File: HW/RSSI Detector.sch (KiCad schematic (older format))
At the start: 13 parts

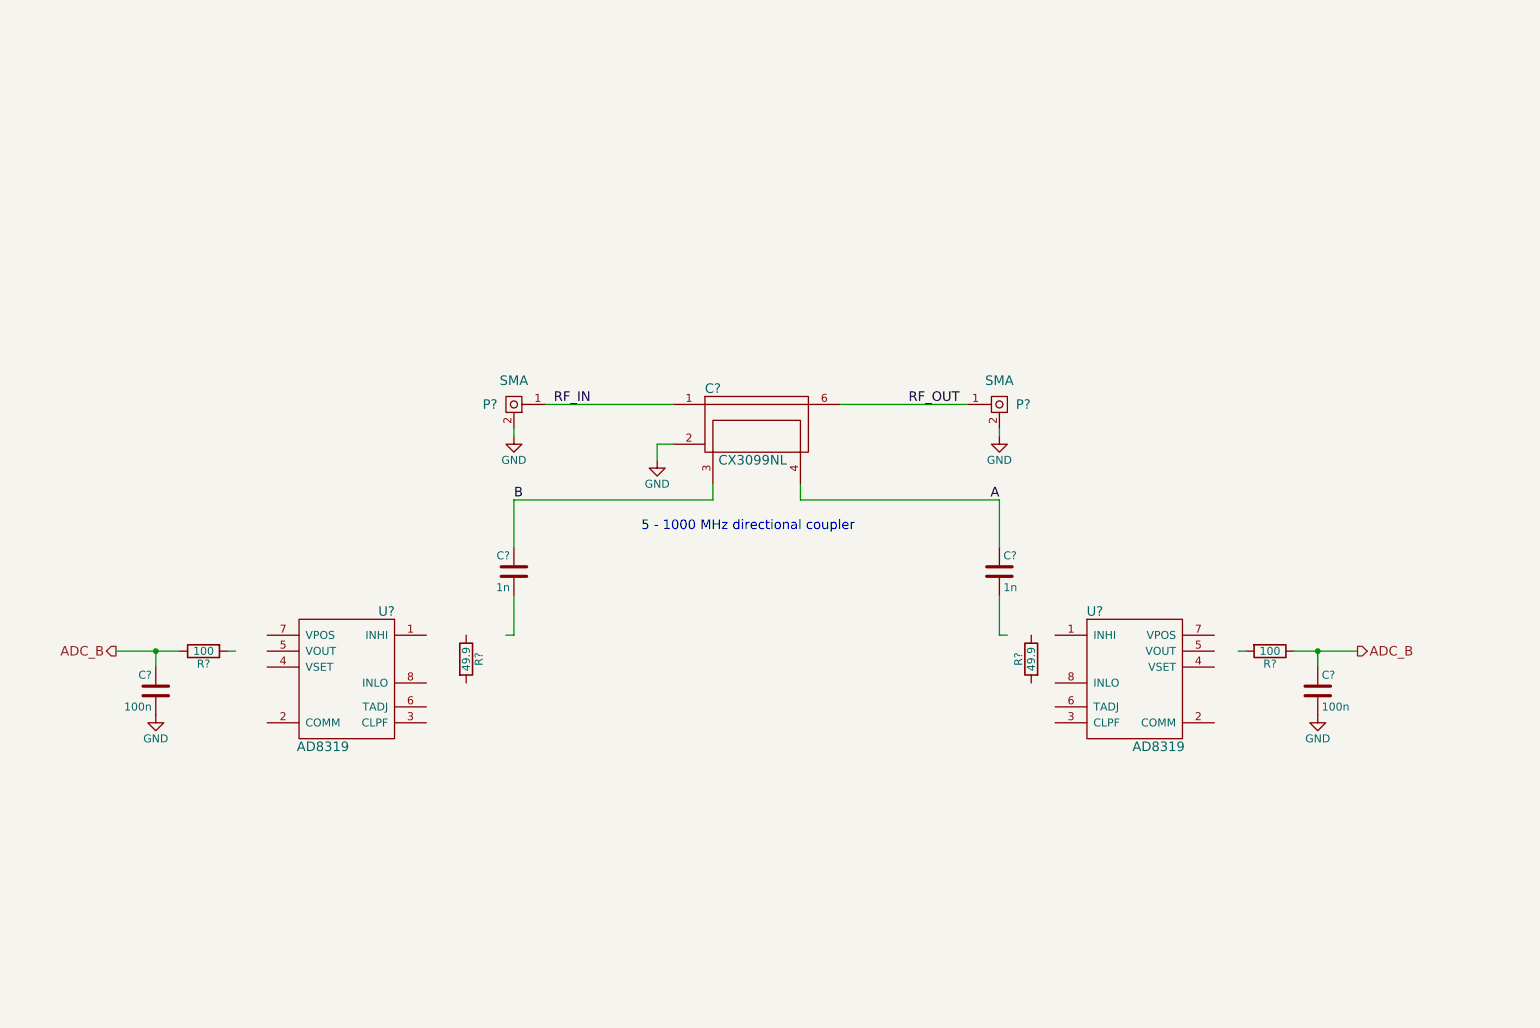
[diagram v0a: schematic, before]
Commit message: finished sch, footprints done
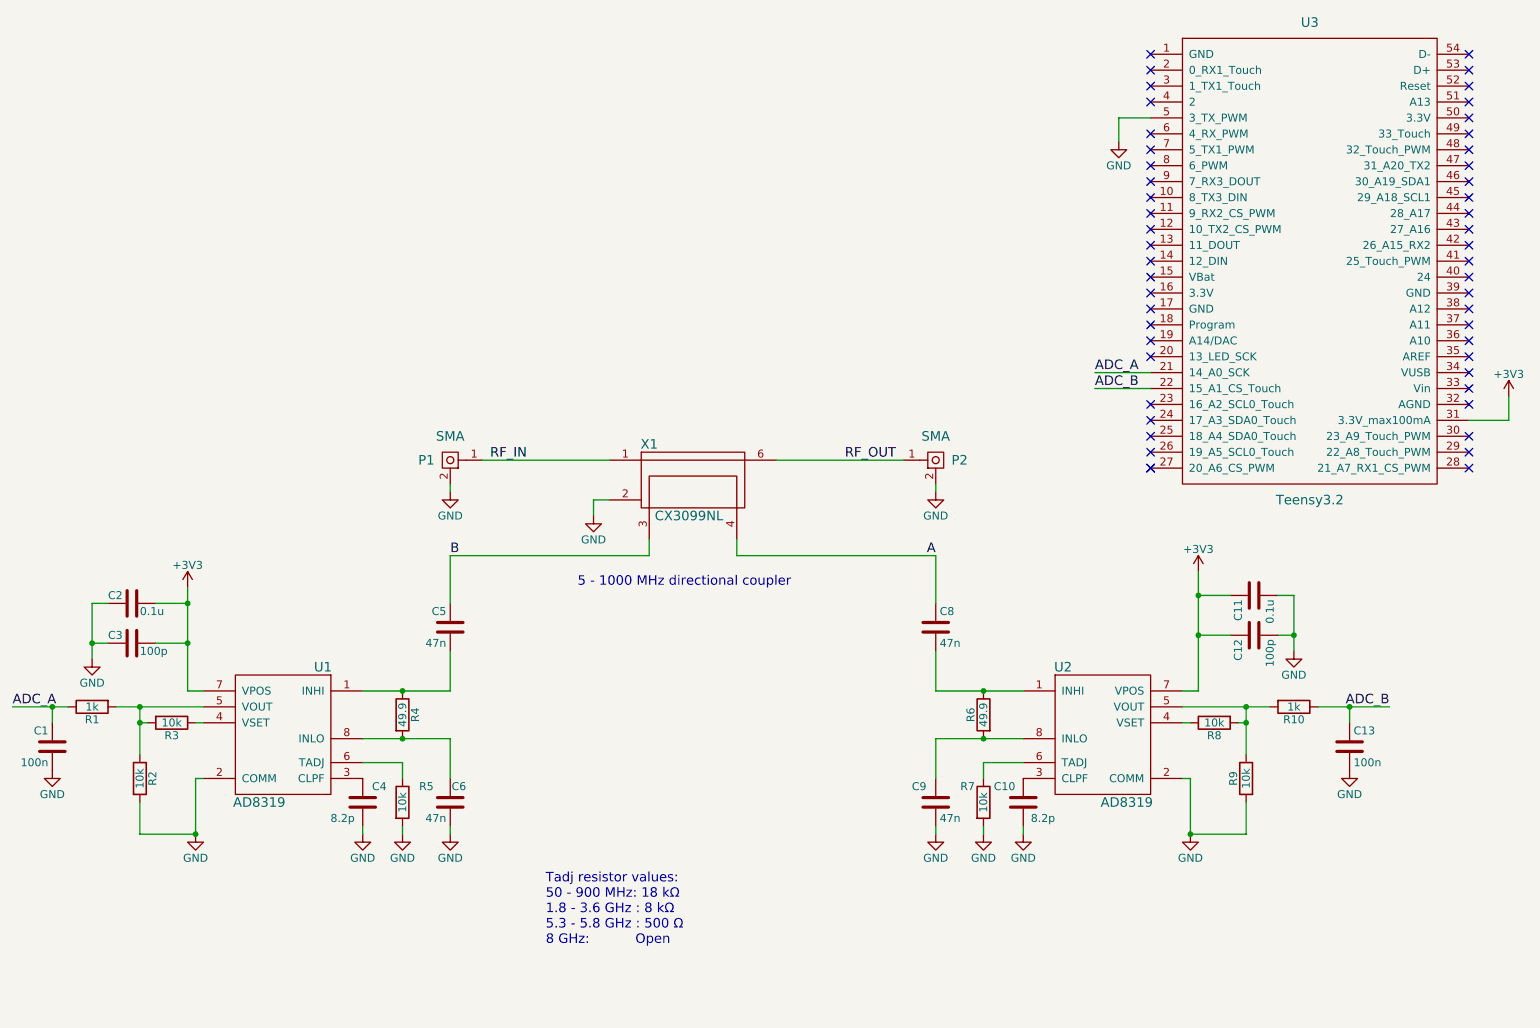
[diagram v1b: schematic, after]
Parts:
- added C10, C4: 8.2p, vna:C_0402b, symbol C
- added C11, C2: 0.1u, vna:C_0603b, symbol C
- added C12, C3: 100p, vna:C_0402b, symbol C
- added C6, C9: 47n, VNA:C_0402b, symbol C
- added R2, R3, R5, R7, R8, R9: 10k, vna:R_0603b, symbol R
- added U3: Teensy3.2, vna:Teensy30_31_32_LC_modified, symbol Teensy3.2
- C1, C13: renamed from C?; footprint VNA:C_0402b -> vna:C_0603b
- C5, C8: renamed from C?; value 1n -> 47n
- P1, P2: renamed from P?; footprint (none) -> vna:CONSMA003.062
- R1, R10: renamed from R?; value 100 -> 1k
- R4, R6: renamed from R?; footprint Resistors_SMD:R_0603 -> vna:R_0402b
- U1, U2: renamed from U?; footprint (none) -> vna:8-LFCSP_VD
- X1: renamed from C?; footprint (none) -> vna:CX3099NL
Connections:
- net labels added: +3V3, ADC_A
- wire segments 22 -> 70
- no-connect marks 0 -> 51
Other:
- note added: "Tadj resistor values:\n50 - 900 MHz: 18 kΩ\n1.8 - 3.6 GHz : 8 kΩ\n5.3 - 5.8 GHz : 500 Ω\n8 GHz: Open"
- moved on the sheet: C1, C13, C5, C8, P1, P2, R1, R10, R4, R6, U1, U2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

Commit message: prelim placement
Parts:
- C10, C12, C3, C4: footprint vna:C_0402b -> vna:C_0603b
- C5, C6, C8, C9: footprint VNA:C_0402b -> vna:C_0402b
- R1, R10: footprint VNA:R_0402b -> Resistors_SMD:R_0603
- R2, R3, R5, R7, R8, R9: footprint vna:R_0603b -> Resistors_SMD:R_0603
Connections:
- net A: now also C8.2, R6.1; no longer C8.1
- net B: now also R4.1
- net GND: now also C6.1, R4.2, R6.2; no longer C6.2
- net at C5.2, U1.1 (INHI): no longer R4.1
- net at C9.1, U2.8 (INLO): no longer R6.2
- new net: C8.1, U2.1 (INHI)
- new net: C6.2, U1.8 (INLO)
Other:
- moved on the sheet: C5, C6, C8, C9, R4, R6
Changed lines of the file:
@@
 L R R4
 U 1 1 59C23EFC
-P 3900 5050
-F 0 "R4" V 3980 5050 50  0000 C CNN
-F 1 "49.9" V 3900 5050 50  0000 C CNN
-F 2 "vna:R_0402b" V 3830 5050 30  0001 C CNN
-F 3 "" H 3900 5050 30  0000 C CNN
-	1    3900 5050
+P 4200 5050
+F 0 "R4" V 4280 5050 50  0000 C CNN
+F 1 "49.9" V 4200 5050 50  0000 C CNN
+F 2 "vna:R_0402b" V 4130 5050 30  0001 C CNN
+F 3 "" H 4200 5050 30  0000 C CNN
+	1    4200 5050
 	1    0    0    -1
 $EndComp
@@
 A
 $Comp
-L C C8
-U 1 1 59C23F21
-P 7250 4500
-F 0 "C8" H 7275 4600 50  0000 L CNN
-F 1 "47n" H 7275 4400 50  0000 L CNN
-F 2 "VNA:C_0402b" H 7288 4350 30  0001 C CNN
-F 3 "" H 7250 4500 60  0000 C CNN
-	1    7250 4500
-	1    0    0    -1
-$EndComp
-$Comp
-L C C5
-U 1 1 59C23F6A
-P 4200 4500
-F 0 "C5" H 4225 4600 50  0000 L CNN
-F 1 "47n" H 4225 4400 50  0000 L CNN
-F 2 "VNA:C_0402b" H 4238 4350 30  0001 C CNN
-F 3 "" H 4200 4500 60  0000 C CNN
-	1    4200 4500
-	-1   0    0    -1
-$EndComp
-$Comp
 L R R1
 U 1 1 59C23F92
@@
 F 0 "R1" V 2030 5000 50  0000 C CNN
 F 1 "1k" V 1950 5000 50  0000 C CNN
-F 2 "VNA:R_0402b" V 1880 5000 30  0001 C CNN
+F 2 "Resistors_SMD:R_0603" V 1880 5000 30  0001 C CNN
 F 3 "" H 1950 5000 30  0000 C CNN
 	1    1950 5000
@@
 L R R6
 U 1 1 59C2507D
-P 7550 5050
-F 0 "R6" V 7630 5050 50  0000 C CNN
-F 1 "49.9" V 7550 5050 50  0000 C CNN
-F 2 "vna:R_0402b" V 7480 5050 30  0001 C CNN
-F 3 "" H 7550 5050 30  0000 C CNN
-	1    7550 5050
+P 7250 5050
+F 0 "R6" V 7330 5050 50  0000 C CNN
+F 1 "49.9" V 7250 5050 50  0000 C CNN
+F 2 "vna:R_0402b" V 7180 5050 30  0001 C CNN
+F 3 "" H 7250 5050 30  0000 C CNN
+	1    7250 5050
 	-1   0    0    -1
 $EndComp
@@
 F 0 "R10" V 9580 5000 50  0000 C CNN
 F 1 "1k" V 9500 5000 50  0000 C CNN
-F 2 "VNA:R_0402b" V 9430 5000 30  0001 C CNN
+F 2 "Resistors_SMD:R_0603" V 9430 5000 30  0001 C CNN
 F 3 "" H 9500 5000 30  0000 C CNN
 	1    9500 5000
@@
 F 0 "C3" V 2150 4450 50  0000 L CNN
 F 1 "100p" V 2250 4650 50  0000 L CNN
-F 2 "vna:C_0402b" H 2238 4450 50  0001 C CNN
+F 2 "vna:C_0603b" H 2238 4450 50  0001 C CNN
 F 3 "" H 2200 4600 50  0001 C CNN
 	1    2200 4600
@@
 	6000 3950 6000 4050
 Wire Wire Line
-	7250 4650 7250 4900
-Wire Wire Line
-	7250 4900 7800 4900
+	7250 4050 7250 4900
 Wire Wire Line
 	6000 4050 7250 4050
 Wire Wire Line
-	7250 4050 7250 4350
-Wire Wire Line
-	4200 4900 4200 4650
-Wire Wire Line
-	3650 4900 4200 4900
+	4200 4050 4200 4900
 Wire Wire Line
 	2100 5000 2650 5000
@@
 Wire Wire Line
 	5450 4050 4200 4050
-Wire Wire Line
-	4200 4050 4200 4350
 Wire Wire Line
 	1700 5000 1700 5100
@@
 Wire Wire Line
 	4200 3600 4200 3650
-Connection ~ 3900 4900
-Wire Wire Line
-	3650 5200 4200 5200
-Connection ~ 7550 4900
-Wire Wire Line
-	7250 5200 7800 5200
+Connection ~ 4200 4900
+Connection ~ 7250 4900
+Wire Wire Line
+	7250 5200 7400 5200
 Wire Wire Line
 	2650 5100 2600 5100
@@
 F 0 "C12" H 9275 4650 50  0000 L CNN
 F 1 "100p" H 9275 4450 50  0000 L CNN
-F 2 "vna:C_0402b" H 9288 4400 50  0001 C CNN
+F 2 "vna:C_0603b" H 9288 4400 50  0001 C CNN
 F 3 "" H 9250 4550 50  0001 C CNN
 	1    9250 4550
@@
 L C C6
 U 1 1 59C28F3F
-P 4200 5600
-F 0 "C6" H 4100 5700 50  0000 L CNN
-F 1 "47n" H 4225 5500 50  0000 L CNN
-F 2 "VNA:C_0402b" H 4238 5450 30  0001 C CNN
-F 3 "" H 4200 5600 60  0000 C CNN
-	1    4200 5600
-	-1   0    0    -1
-$EndComp
-Wire Wire Line
-	4200 5200 4200 5450
-Connection ~ 3900 5200
+P 3850 5200
+F 0 "C6" H 3750 5300 50  0000 L CNN
+F 1 "47n" H 3875 5100 50  0000 L CNN
+F 2 "vna:C_0402b" H 3888 5050 30  0001 C CNN
+F 3 "" H 3850 5200 60  0000 C CNN
+	1    3850 5200
+	0    1    -1   0
+$EndComp
+Wire Wire Line
+	4200 5200 4200 5800
+Connection ~ 4200 5200
 $Comp
 L C C9
 U 1 1 59C29280
-P 7250 5600
-F 0 "C9" H 7100 5700 50  0000 L CNN
-F 1 "47n" H 7275 5500 50  0000 L CNN
-F 2 "VNA:C_0402b" H 7288 5450 30  0001 C CNN
-F 3 "" H 7250 5600 60  0000 C CNN
-	1    7250 5600
-	1    0    0    -1
-$EndComp
-Wire Wire Line
-	7250 5200 7250 5450
-Connection ~ 7550 5200
+P 7550 5200
+F 0 "C9" H 7400 5300 50  0000 L CNN
+F 1 "47n" H 7575 5100 50  0000 L CNN
+F 2 "vna:C_0402b" H 7588 5050 30  0001 C CNN
+F 3 "" H 7550 5200 60  0000 C CNN
+	1    7550 5200
+	0    1    1    0
+$EndComp
+Wire Wire Line
+	7250 5200 7250 5800
+Connection ~ 7250 5200
 $Comp
 L R R5
@@
 F 0 "R5" H 4050 5700 50  0000 C CNN
 F 1 "10k" V 3900 5600 50  0000 C CNN
-F 2 "vna:R_0603b" V 3830 5600 30  0001 C CNN
+F 2 "Resistors_SMD:R_0603" V 3830 5600 30  0001 C CNN
 F 3 "" H 3900 5600 30  0000 C CNN
 	1    3900 5600
@@
 F 0 "R7" H 7450 5700 50  0000 C CNN
 F 1 "10k" V 7550 5600 50  0000 C CNN
-F 2 "vna:R_0603b" V 7480 5600 30  0001 C CNN
+F 2 "Resistors_SMD:R_0603" V 7480 5600 30  0001 C CNN
 F 3 "" H 7550 5600 30  0000 C CNN
 	1    7550 5600
@@
 F 0 "R2" V 2330 5450 50  0000 C CNN
 F 1 "10k" V 2250 5450 50  0000 C CNN
-F 2 "vna:R_0603b" V 2180 5450 30  0001 C CNN
+F 2 "Resistors_SMD:R_0603" V 2180 5450 30  0001 C CNN
 F 3 "" H 2250 5450 30  0000 C CNN
 	1    2250 5450
@@
 F 0 "R3" V 2530 5100 50  0000 C CNN
 F 1 "10k" V 2450 5100 50  0000 C CNN
-F 2 "vna:R_0603b" V 2380 5100 30  0001 C CNN
+F 2 "Resistors_SMD:R_0603" V 2380 5100 30  0001 C CNN
 F 3 "" H 2450 5100 30  0000 C CNN
 	1    2450 5100
@@
 F 0 "R9" V 9280 5450 50  0000 C CNN
 F 1 "10k" V 9200 5450 50  0000 C CNN
-F 2 "vna:R_0603b" V 9130 5450 30  0001 C CNN
+F 2 "Resistors_SMD:R_0603" V 9130 5450 30  0001 C CNN
 F 3 "" H 9200 5450 30  0000 C CNN
 	1    9200 5450
@@
 F 0 "R8" V 9080 5100 50  0000 C CNN
 F 1 "10k" V 9000 5100 50  0000 C CNN
-F 2 "vna:R_0603b" V 8930 5100 30  0001 C CNN
+F 2 "Resistors_SMD:R_0603" V 8930 5100 30  0001 C CNN
 F 3 "" H 9000 5100 30  0000 C CNN
 	1    9000 5100
@@
 F 0 "C4" H 3500 5500 50  0000 L CNN
 F 1 "8.2p" H 3700 5700 50  0000 L CNN
-F 2 "vna:C_0402b" H 3688 5450 50  0001 C CNN
+F 2 "vna:C_0603b" H 3688 5450 50  0001 C CNN
 F 3 "" H 3650 5600 50  0001 C CNN
 	1    3650 5600
@@
 F 0 "C10" H 7850 5500 50  0000 L CNN
 F 1 "8.2p" H 7600 5700 50  0000 L CNN
-F 2 "vna:C_0402b" H 7838 5450 50  0001 C CNN
+F 2 "vna:C_0603b" H 7838 5450 50  0001 C CNN
 F 3 "" H 7800 5600 50  0001 C CNN
 	1    7800 5600
@@
 Wire Wire Line
 	3900 5750 3900 5800
-Wire Wire Line
-	4200 5750 4200 5800
 $Comp
 L GND #PWR014
@@
 Wire Wire Line
 	7550 5750 7550 5800
-Wire Wire Line
-	7250 5750 7250 5800
 Wire Wire Line
 	8800 5450 8850 5450
@@
 NoConn ~ 8600 3300
 NoConn ~ 8600 3400
+$Comp
+L C C5
+U 1 1 59C23F6A
+P 3850 4900
+F 0 "C5" H 3875 5000 50  0000 L CNN
+F 1 "47n" H 3875 4800 50  0000 L CNN
+F 2 "vna:C_0402b" H 3888 4750 30  0001 C CNN
+F 3 "" H 3850 4900 60  0000 C CNN
+	1    3850 4900
+	0    1    -1   0
+$EndComp
+Wire Wire Line
+	4200 4900 4000 4900
+Wire Wire Line
+	3700 4900 3650 4900
+Wire Wire Line
+	3650 5200 3700 5200
+Wire Wire Line
+	4000 5200 4200 5200
+$Comp
+L C C8
+U 1 1 59C23F21
+P 7550 4900
+F 0 "C8" H 7575 5000 50  0000 L CNN
+F 1 "47n" H 7575 4800 50  0000 L CNN
+F 2 "vna:C_0402b" H 7588 4750 30  0001 C CNN
+F 3 "" H 7550 4900 60  0000 C CNN
+	1    7550 4900
+	0    1    1    0
+$EndComp
+Wire Wire Line
+	7250 4900 7400 4900
+Wire Wire Line
+	7700 4900 7800 4900
+Wire Wire Line
+	7700 5200 7800 5200
 $EndSCHEMATC

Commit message: put Henrik's coupler
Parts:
- removed X1: CX3099NL, vna:CX3099NL, symbol CX3099NL
- added F?: COUPLER, symbol COUPLER
- added R? (x2): 49.9, vna:R_0402b, symbol R
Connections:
- net A: now also F?.6
- net B: now also F?.3
- net GND: now also F?.GND, R?.2, R?.2
- net RF_IN: now also F?.1
- net RF_OUT: now also F?.2
- new net: F?.4, R?.1
- new net: F?.5, R?.1
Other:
- note removed: "5 - 1000 MHz directional coupler"
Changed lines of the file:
@@
 $EndComp
-$Comp
-L CX3099NL X1
-U 1 1 59C262AE
-P 5750 3550
-F 0 "X1" H 5450 3750 60  0000 C CNN
-F 1 "CX3099NL" H 5700 3300 60  0000 C CNN
-F 2 "vna:CX3099NL" H 5750 3650 60  0001 C CNN
-F 3 "" H 5750 3650 60  0000 C CNN
-	1    5750 3550
-	1    0    0    -1
-$EndComp
-Text Notes 5000 4250 0    60   ~ 0
-5 - 1000 MHz directional coupler
 $Comp
 L SMA P1
@@
 Wire Wire Line
 	7700 5200 7800 5200
+$Comp
+L COUPLER F?
+U 1 1 59CC1068
+P 5750 3550
+F 0 "F?" H 6200 3400 60  0000 C CNN
+F 1 "COUPLER" H 5650 3800 60  0000 C CNN
+F 2 "" H 5750 3650 60  0000 C CNN
+F 3 "" H 5750 3650 60  0000 C CNN
+	1    5750 3550
+	1    0    0    -1
+$EndComp
+$Comp
+L R R?
+U 1 1 59CC14B8
+P 5650 4200
+F 0 "R?" V 5730 4200 50  0000 C CNN
+F 1 "49.9" V 5650 4200 50  0000 C CNN
+F 2 "vna:R_0402b" V 5580 4200 30  0001 C CNN
+F 3 "" H 5650 4200 30  0000 C CNN
+	1    5650 4200
+	1    0    0    -1
+$EndComp
+$Comp
+L R R?
+U 1 1 59CC1563
+P 5800 4200
+F 0 "R?" V 5880 4200 50  0000 C CNN
+F 1 "49.9" V 5800 4200 50  0000 C CNN
+F 2 "vna:R_0402b" V 5730 4200 30  0001 C CNN
+F 3 "" H 5800 4200 30  0000 C CNN
+	1    5800 4200
+	1    0    0    -1
+$EndComp
+Wire Wire Line
+	5650 3950 5650 4050
+Wire Wire Line
+	5800 3950 5800 4050
+Wire Wire Line
+	5650 4350 5650 4400
+Wire Wire Line
+	5800 4350 5800 4400
+$Comp
+L GND #PWR?
+U 1 1 59CC1D5F
+P 5650 4400
+F 0 "#PWR?" H 5650 4150 50  0001 C CNN
+F 1 "GND" H 5650 4250 50  0000 C CNN
+F 2 "" H 5650 4400 60  0000 C CNN
+F 3 "" H 5650 4400 60  0000 C CNN
+	1    5650 4400
+	-1   0    0    -1
+$EndComp
+$Comp
+L GND #PWR?
+U 1 1 59CC2094
+P 5800 4400
+F 0 "#PWR?" H 5800 4150 50  0001 C CNN
+F 1 "GND" H 5800 4250 50  0000 C CNN
+F 2 "" H 5800 4400 60  0000 C CNN
+F 3 "" H 5800 4400 60  0000 C CNN
+	1    5800 4400
+	-1   0    0    -1
+$EndComp
 $EndSCHEMATC

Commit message: layout done
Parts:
- F1: renamed from F?; footprint (none) -> vna:coupler4
- gave numbers to parts that had none: 2
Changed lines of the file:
@@
 	7700 5200 7800 5200
 $Comp
-L COUPLER F?
+L COUPLER F1
 U 1 1 59CC1068
 P 5750 3550
-F 0 "F?" H 6200 3400 60  0000 C CNN
+F 0 "F1" H 6200 3400 60  0000 C CNN
 F 1 "COUPLER" H 5650 3800 60  0000 C CNN
-F 2 "" H 5750 3650 60  0000 C CNN
+F 2 "vna:coupler4" H 5750 3650 60  0001 C CNN
 F 3 "" H 5750 3650 60  0000 C CNN
 	1    5750 3550
@@
 $EndComp
 $Comp
-L R R?
+L R R11
 U 1 1 59CC14B8
 P 5650 4200
-F 0 "R?" V 5730 4200 50  0000 C CNN
+F 0 "R11" V 5730 4200 50  0000 C CNN
 F 1 "49.9" V 5650 4200 50  0000 C CNN
 F 2 "vna:R_0402b" V 5580 4200 30  0001 C CNN
@@
 $EndComp
 $Comp
-L R R?
+L R R12
 U 1 1 59CC1563
 P 5800 4200
-F 0 "R?" V 5880 4200 50  0000 C CNN
+F 0 "R12" V 5880 4200 50  0000 C CNN
 F 1 "49.9" V 5800 4200 50  0000 C CNN
 F 2 "vna:R_0402b" V 5730 4200 30  0001 C CNN
@@
 	5800 4350 5800 4400
 $Comp
-L GND #PWR?
+L GND #PWR020
 U 1 1 59CC1D5F
 P 5650 4400
-F 0 "#PWR?" H 5650 4150 50  0001 C CNN
+F 0 "#PWR020" H 5650 4150 50  0001 C CNN
 F 1 "GND" H 5650 4250 50  0000 C CNN
 F 2 "" H 5650 4400 60  0000 C CNN
@@
 $EndComp
 $Comp
-L GND #PWR?
+L GND #PWR021
 U 1 1 59CC2094
 P 5800 4400
-F 0 "#PWR?" H 5800 4150 50  0001 C CNN
+F 0 "#PWR021" H 5800 4150 50  0001 C CNN
 F 1 "GND" H 5800 4250 50  0000 C CNN
 F 2 "" H 5800 4400 60  0000 C CNN
